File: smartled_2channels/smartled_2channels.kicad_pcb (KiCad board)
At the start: 2 copper layers, 83 x 16 mm, 92 parts, among them J2 Conn_01x02, Q1 Q_NMOS_GSD, SW1 SW_Push, U1 OC5028B, U2 MAX485E, U3 PY32F003F1xUx, U4 OC5864, U5 SGM2033-3.3, U6 OC5028B, U7 GS8521

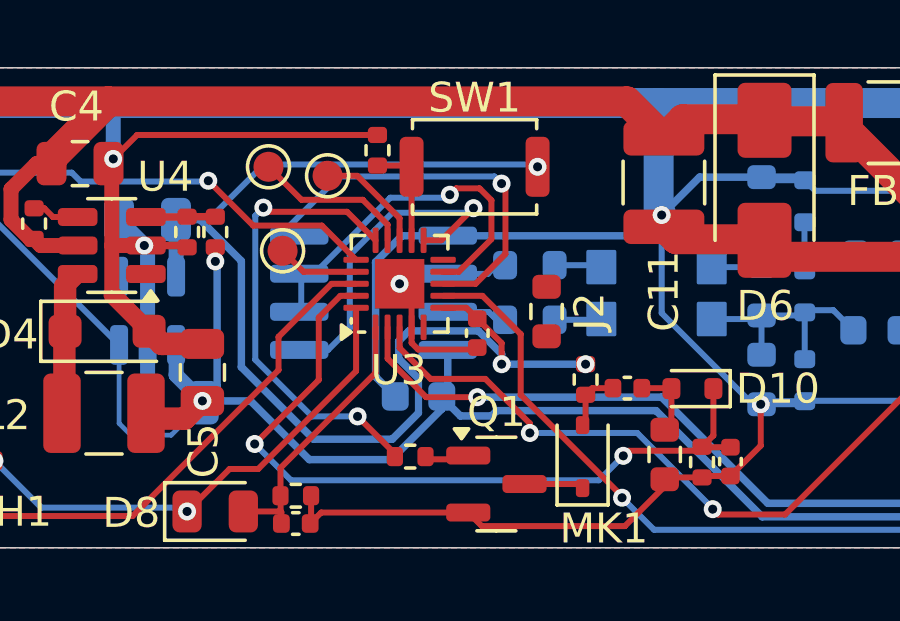
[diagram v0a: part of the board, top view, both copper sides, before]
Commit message: 修改TP焊盘为0.6mm，引出I2C接口
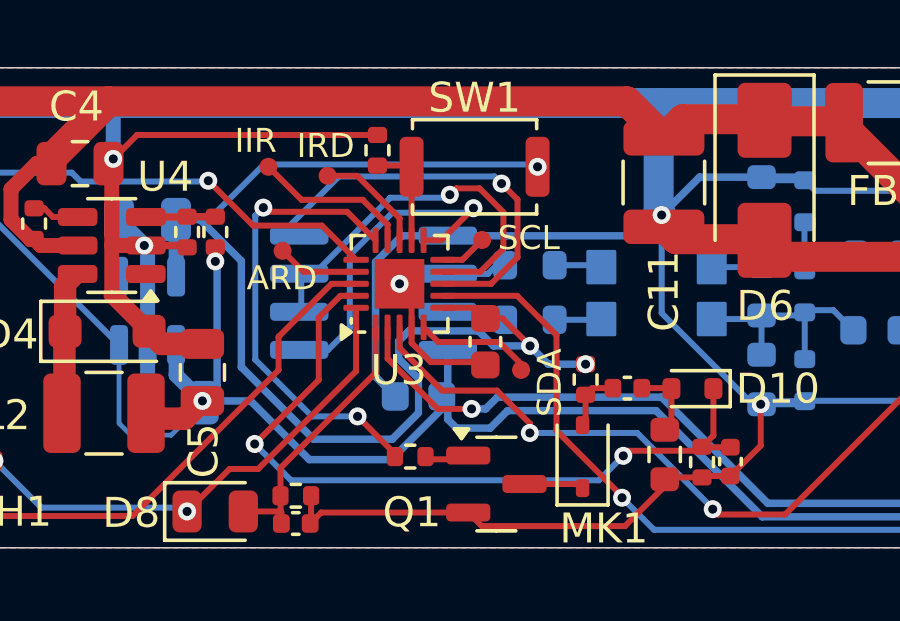
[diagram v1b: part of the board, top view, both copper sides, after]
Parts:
- removed J2: Conn_01x02, Resistor_SMD:R_0603_1608Metric
- added TP8: TestPoint, project_footprints:1Pad_0.6mm, F.Cu at (142.3, 91.8)
- added TP9: TestPoint, project_footprints:1Pad_0.6mm, F.Cu at (143.7, 96.2)
- C16: footprint Capacitor_SMD:C_0402_1005Metric -> Capacitor_SMD:C_0603_1608Metric
- TP1, TP2, TP3: footprint TestPoint:TestPoint_Pad_D1.0mm -> project_footprints:1Pad_0.6mm
- moved C16 0.39 mm to (142.5, 95.2)
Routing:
- net /I2C_SDA: track 0.00 -> 3.95 mm
- net /I2C_SCL: track 0.00 -> 1.57 mm
- net /MAX485_TR: track 12.3 -> 13.1 mm
- net /PWM2: track 45.1 -> 45.8 mm
- net +5V: track 78.9 -> 79.6 mm
- net /MAX485_DI: track 13.2 -> 13.8 mm
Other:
- board text added: "ARD"
- board text added: "IIR"
- board text added: "IRD"
- board text added: "SCL"
- board text added: "SDA"

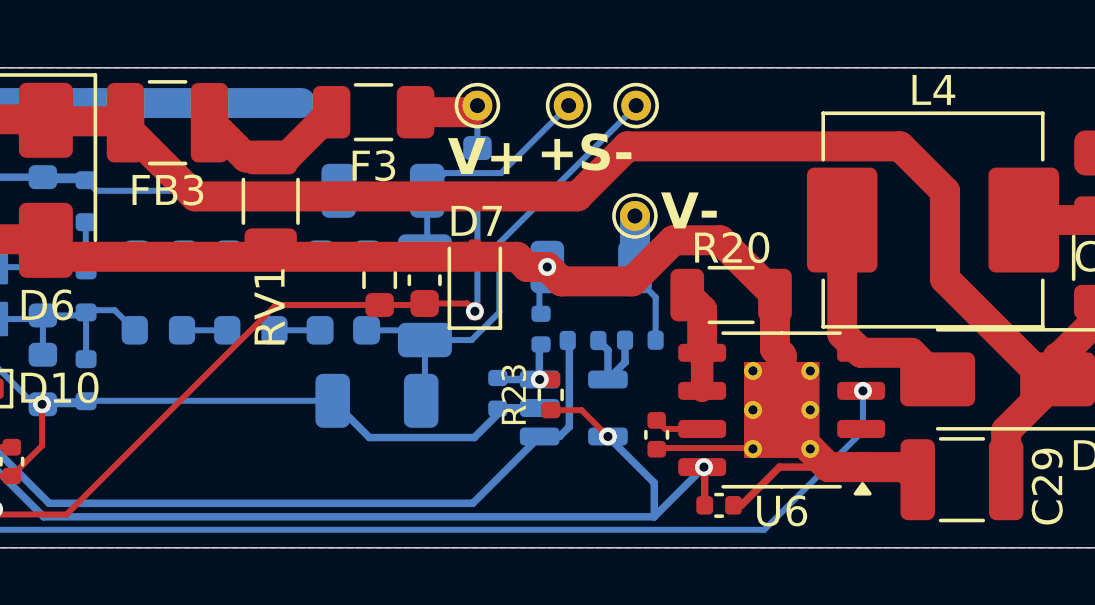
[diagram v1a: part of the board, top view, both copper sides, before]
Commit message: 保险丝移动到负极
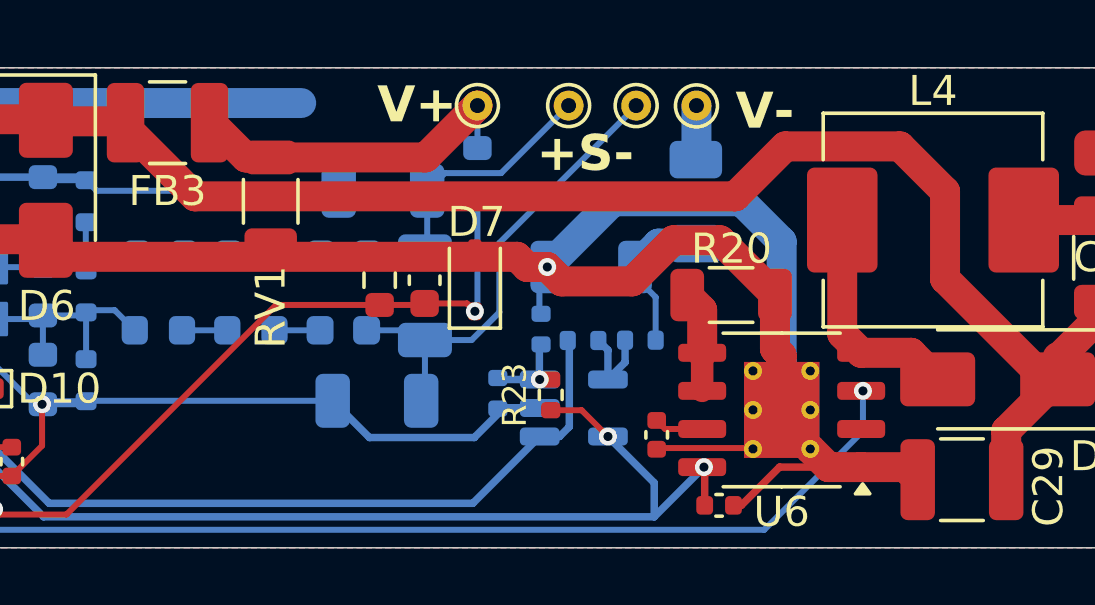
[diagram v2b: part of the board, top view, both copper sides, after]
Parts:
- F3: moved to B.Cu
- moved F3 11.1 mm to (173.4, 90.6), turned to -90 degrees
- moved TP5 4.20 mm to (173.4, 87.4)
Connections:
- F3 pad 1: /VIN+ -> /VIN-
- F3 pad 2: Net-(F3-Pad2) -> /Isamp-
- FB3 pad 1: Net-(F3-Pad2) -> /VIN+
- R12 pad 1: /VIN- -> /Isamp-
- R17 pad 1: /VIN- -> /Isamp-
- RV1 pad 1: Net-(F3-Pad2) -> /VIN+
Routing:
- net GND: track 237.0 -> 251.9 mm
- net /VIN+: track 3.66 -> 12.0 mm
- net Net-(F3-Pad2): track 5.18 -> 0.00 mm
- net /Isamp-: track 0.00 -> 5.08 mm
- net /VIN-: track 4.43 -> 1.81 mm

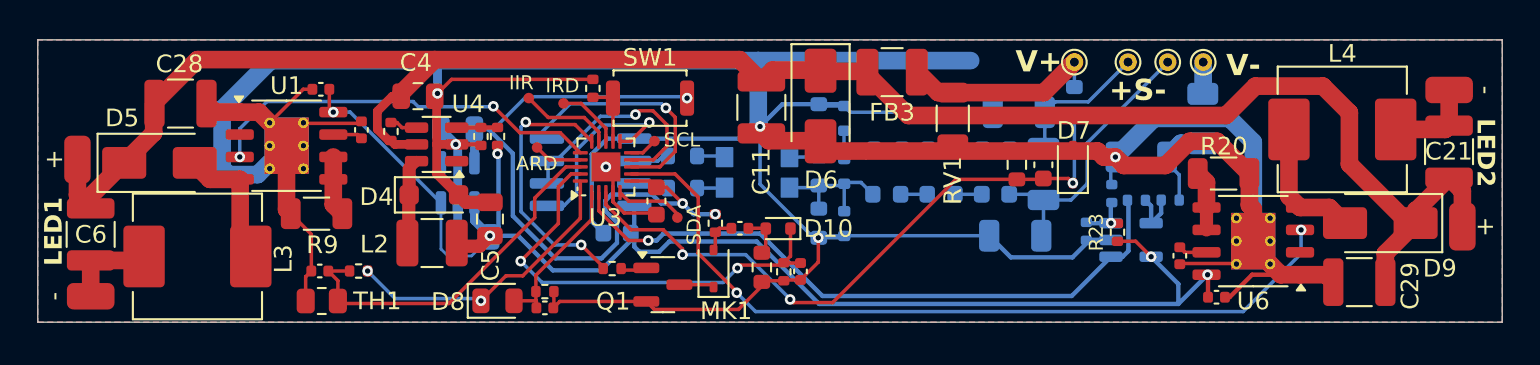
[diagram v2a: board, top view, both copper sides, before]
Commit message: 修改LED输出接口为通孔焊盘
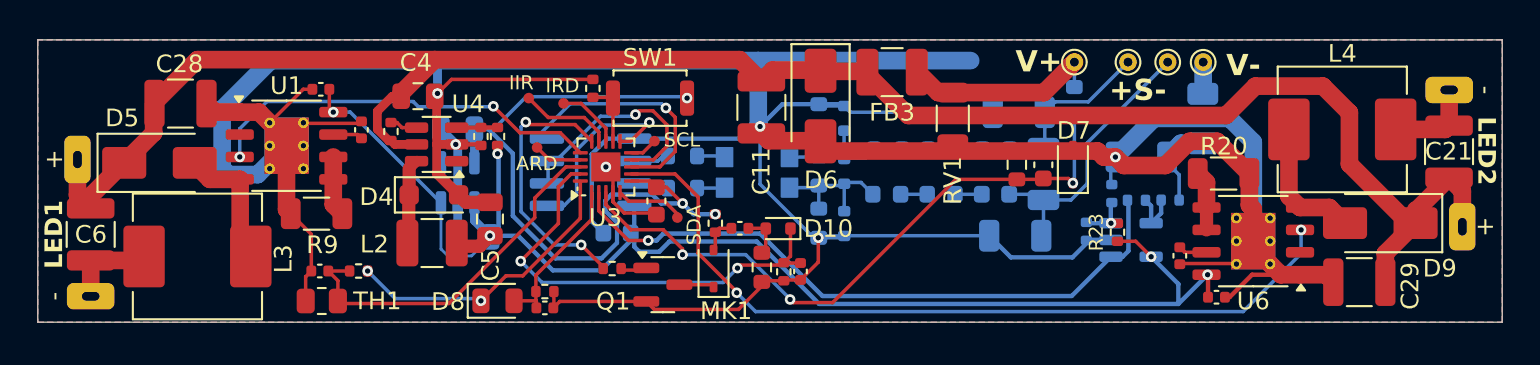
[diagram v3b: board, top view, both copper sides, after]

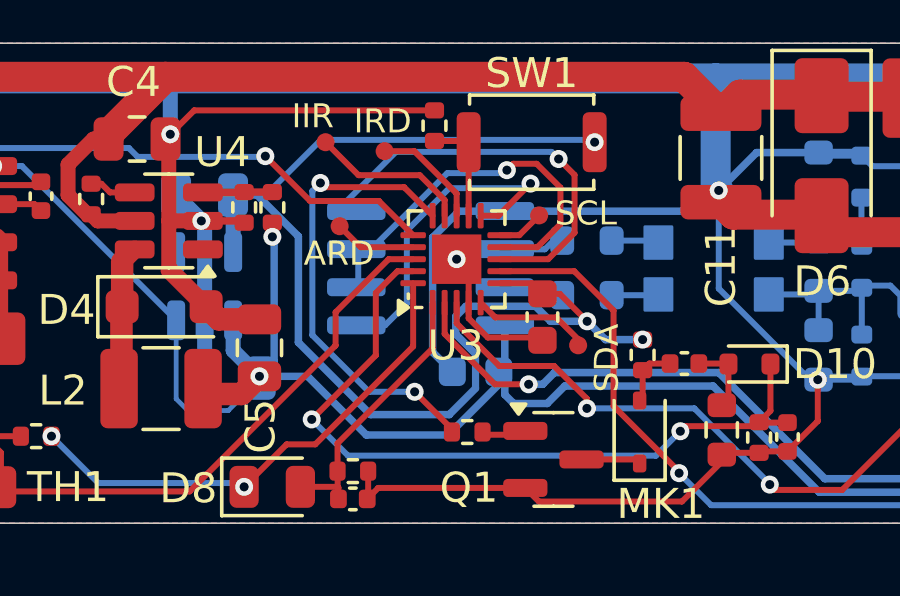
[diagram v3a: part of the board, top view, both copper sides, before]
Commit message: MAX485 RO添加稳压二极管做电平转换
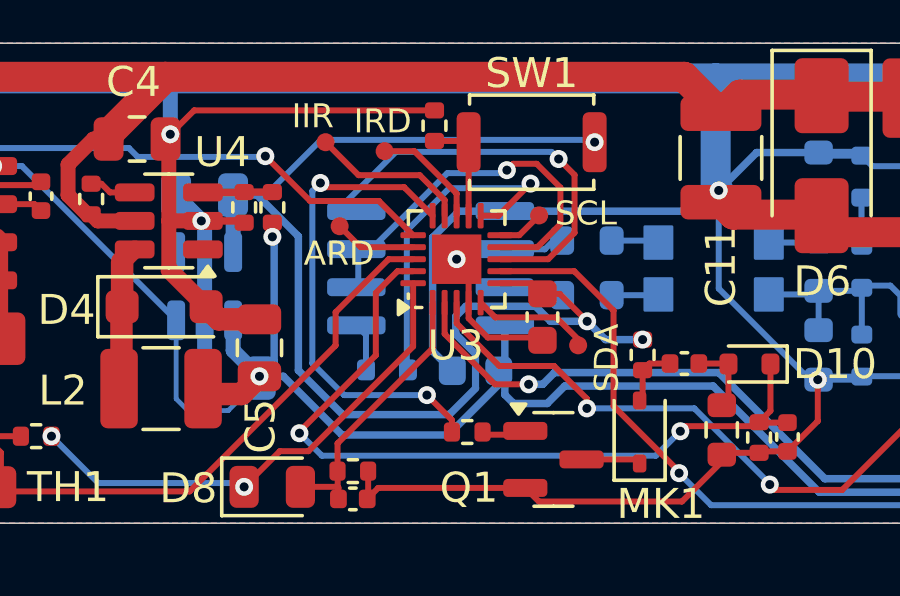
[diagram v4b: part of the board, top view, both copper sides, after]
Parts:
- added D11: 2.0V, Diode_SMD:D_SOD-523, B.Cu at (137.3, 97.0)
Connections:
- U2 pad 1: /MAX485_RO -> Net-(D11-K)
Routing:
- net Net-(D11-K): track 0.00 -> 1.62 mm
- net /ADC_MIC: track 25.6 -> 26.4 mm
- net /DET_EN: track 15.5 -> 16.3 mm
- net +3.3V: track 41.2 -> 41.8 mm
